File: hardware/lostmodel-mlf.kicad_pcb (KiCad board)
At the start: 2 copper layers, 16 x 33.1 mm, 18 parts, among them IC1 ATMEGA88P, K1 CONN_3, K2 G T R, P1 ISP, Q1 BC847C

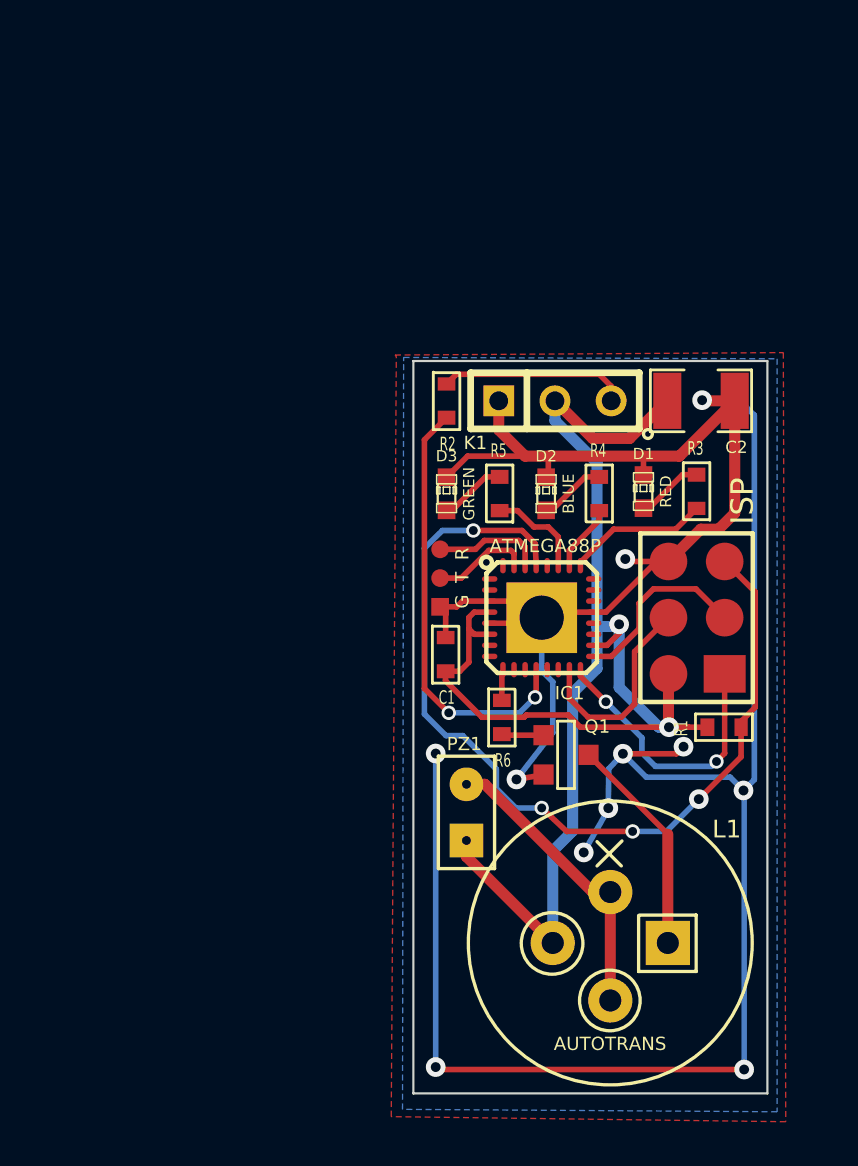
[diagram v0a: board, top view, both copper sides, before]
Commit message: Completing KiCAD upgrade changes
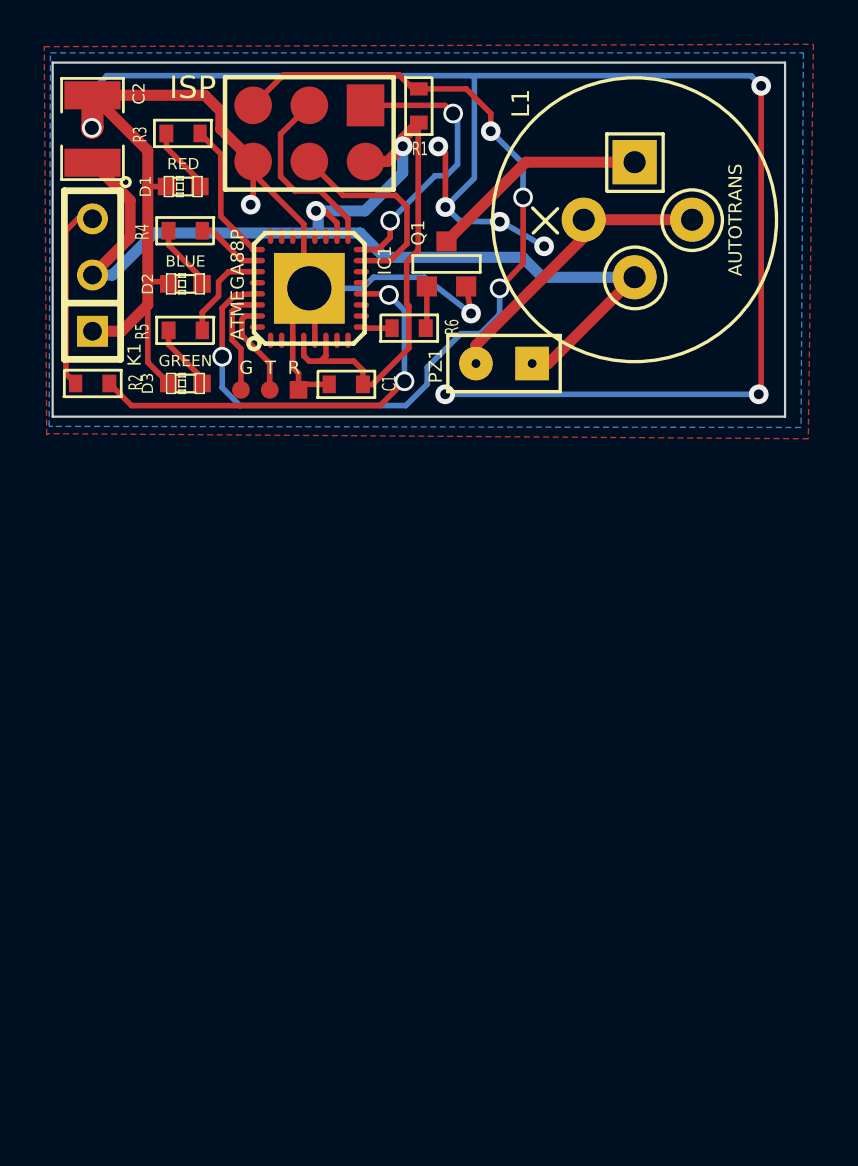
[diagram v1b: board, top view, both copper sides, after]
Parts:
- moved L1 32.7 mm to (69.1, 38.1), turned to 270 degrees
- moved R1 31.3 mm to (59.3, 32.9), turned to 90 degrees
- moved C2 30.1 mm to (44.6, 34.0), turned to 90 degrees
- moved R3 28.3 mm to (48.7, 34.2), turned to 0 degrees
- moved P1 28.0 mm to (54.4, 34.2), turned to 180 degrees
- moved D1 25.0 mm to (48.7, 36.6), turned to 180 degrees
- moved Q1 22.8 mm to (60.6, 40.1), turned to 180 degrees
- moved R4 22.2 mm to (48.8, 38.6), turned to 0 degrees
- moved K1 21.7 mm to (44.6, 40.6), turned to 90 degrees
- moved PZ1 20.4 mm to (63.2, 44.6), turned to 180 degrees
- moved D2 18.9 mm to (48.8, 41.0), turned to 180 degrees
- moved IC1 18.2 mm to (54.4, 41.2), turned to 90 degrees
- moved R6 18.1 mm to (58.9, 43.0), turned to 180 degrees
- moved R2 16.0 mm to (44.6, 45.5), turned to 180 degrees
- moved R5 16.0 mm to (48.8, 43.1), turned to 0 degrees
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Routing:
- net +5V: track 68.0 -> 68.8 mm
- net GND: track 133.4 -> 133.7 mm, vias 11 -> 10
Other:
- board size 16 x 33.1 mm -> 33.1 x 16 mm
- board text added: "Gruvin's Lost Model Alarm v1.2"
- board text added: "github.com/gruvin/lostmodel"
- board text removed: "G9X Lost Model Alarm v1.1"
- board text removed: "lostmodel.googlecode.com"
